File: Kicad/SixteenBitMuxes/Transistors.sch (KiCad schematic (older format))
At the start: 20 parts, among them Q1 PN2222A, Q10 2SC1815, Q12 S9013, Q14 S9018, Q15 BC848B, Q16 2SC1623, Q17 MPSA18, Q19 2N5088, Q2 MMBT3904, Q3 MMBT5551L, Q4 MMBTA42, Q5 BC807, Q6 BC846, Q7 BC847B, Q8 BC847C, Q9 C945, U8 CD4067BM, U9 CD4067BM

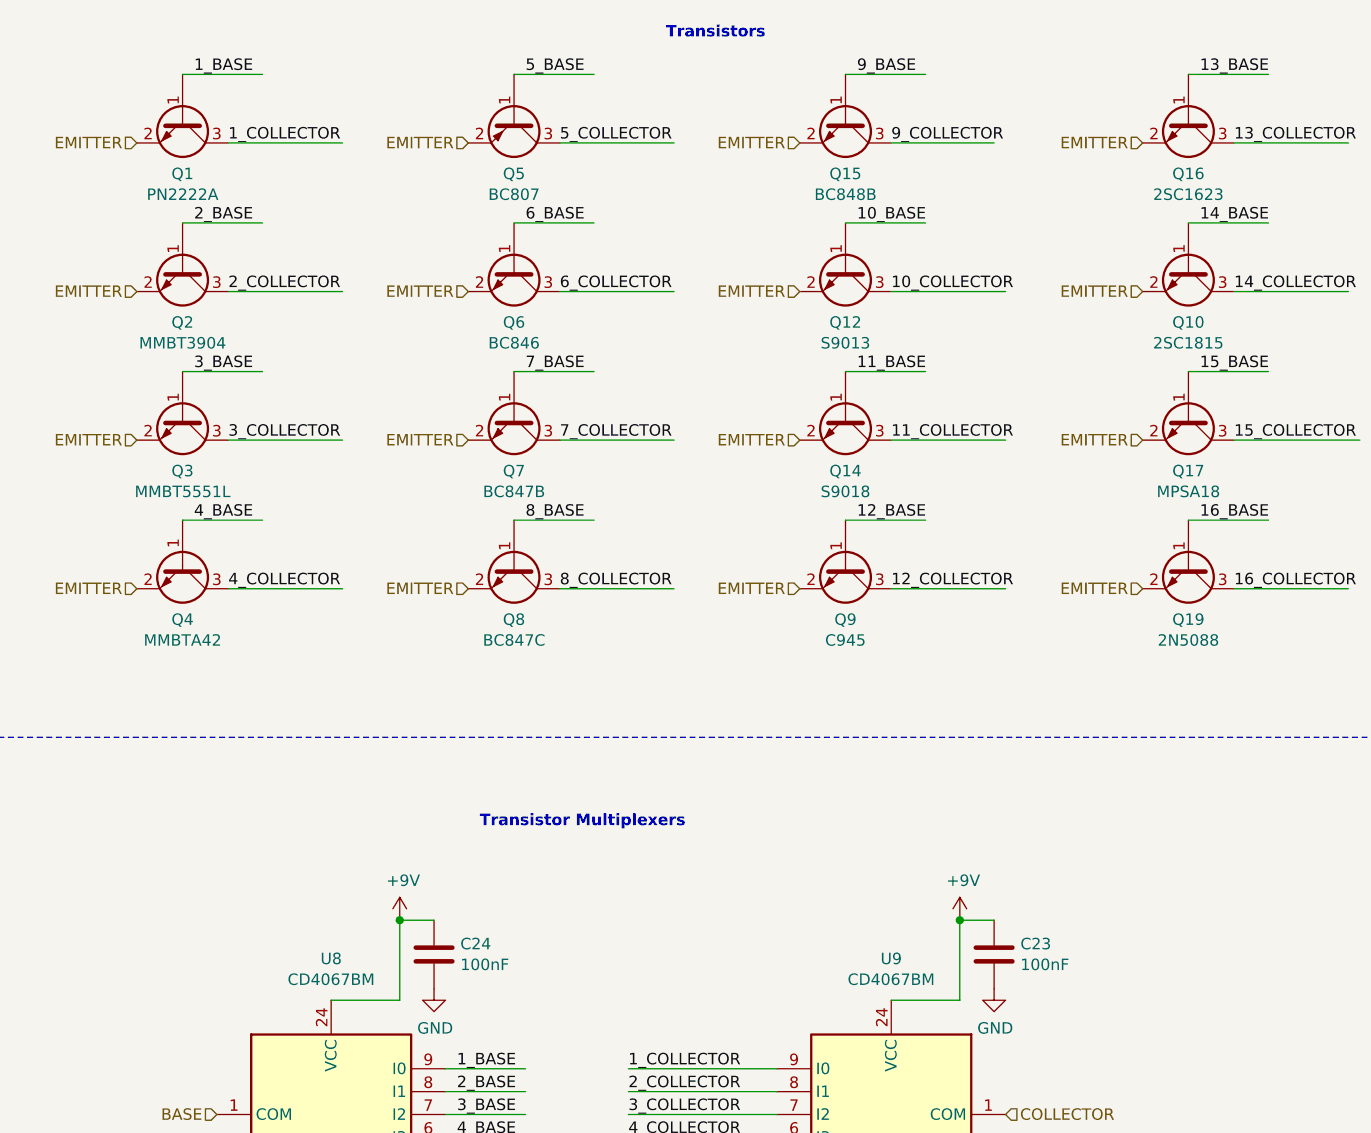
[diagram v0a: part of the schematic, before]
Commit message: PCB Logo/texts
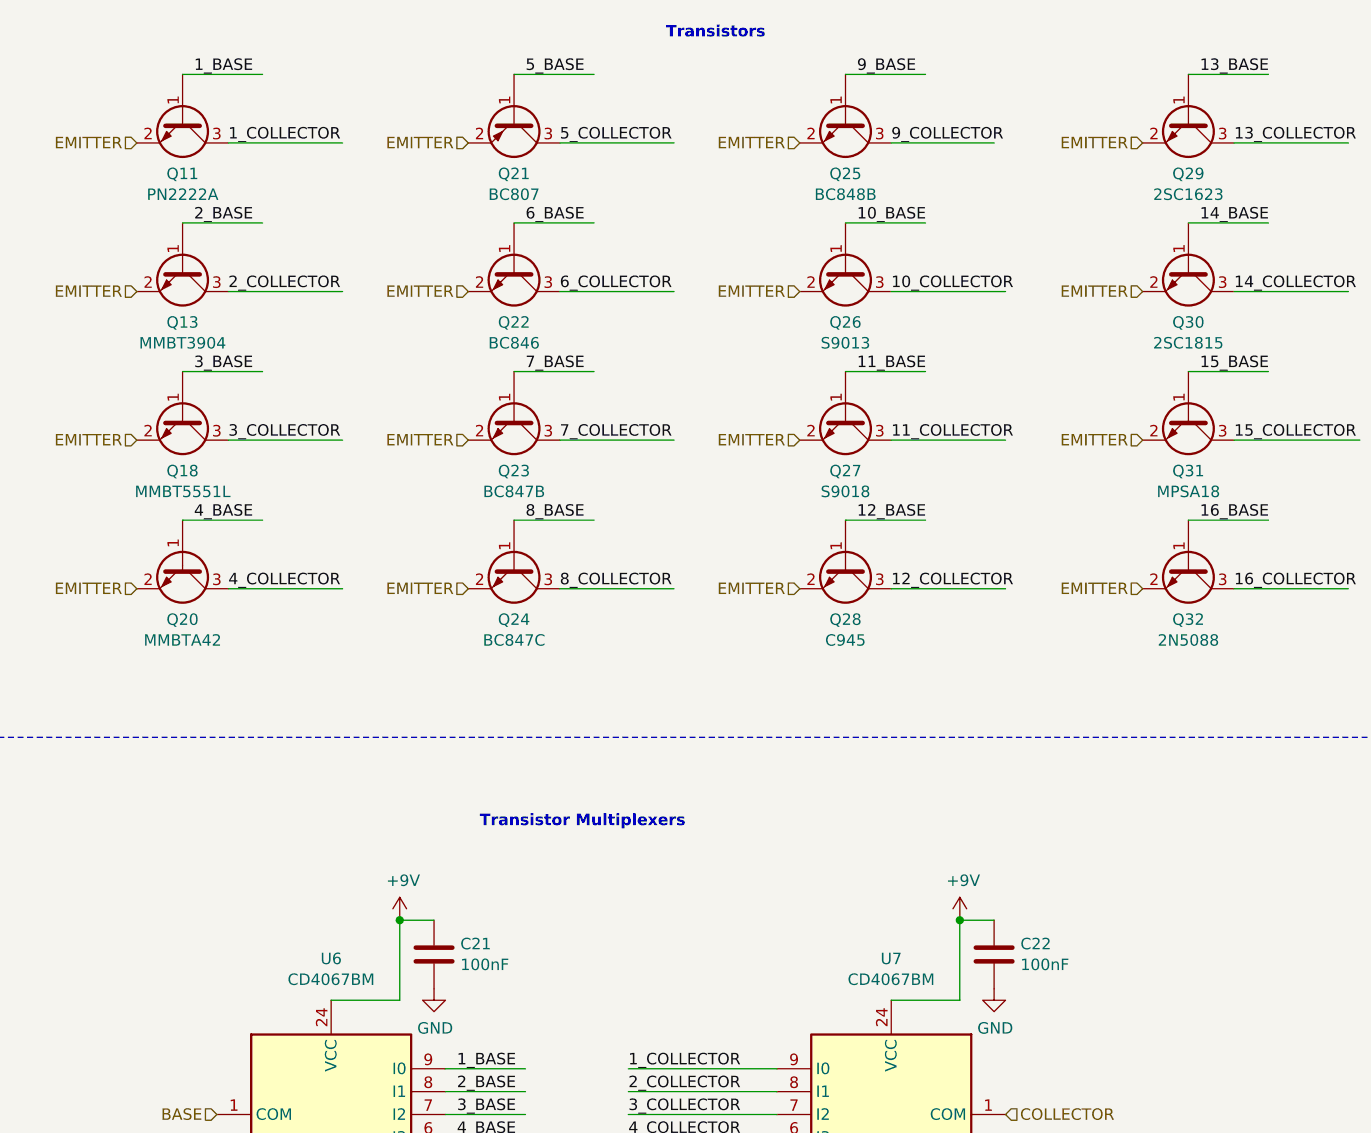
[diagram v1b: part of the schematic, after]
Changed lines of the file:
@@
 $Descr A4 11693 8268
 encoding utf-8
-Sheet 8 9
+Sheet 6 9
 Title "Guitar Pedal Effect Fuzz Digitally Controlled"
 Date "2020-04-07"
@@
 AR Path="/5F9746B8/5EA993A8" Ref="Q24"  Part="1"
 AR Path="/5ED1AB26/5EA993A8" Ref="Q20"  Part="1"
-F 0 "Q4" V 1835 3400 50  0000 C CNN
+F 0 "Q20" V 1835 3400 50  0000 C CNN
 F 1 "MMBTA42" V 1926 3400 50  0000 C CNN
 F 2 "Package_TO_SOT_SMD:SOT-23_Handsoldering" H 1800 3325 50  0001 L CIN
@@
 AR Path="/5F9746B8/5EA993B4" Ref="Q39"  Part="1"
 AR Path="/5ED1AB26/5EA993B4" Ref="Q32"  Part="1"
-F 0 "Q19" V 6235 3400 50  0000 C CNN
+F 0 "Q32" V 6235 3400 50  0000 C CNN
 F 1 "2N5088" V 6326 3400 50  0000 C CNN
 F 2 "Package_TO_SOT_THT:TO-92_Inline" H 6200 3325 50  0001 L CIN
@@
 AR Path="/5F9746B8/5EA993C0" Ref="Q37"  Part="1"
 AR Path="/5ED1AB26/5EA993C0" Ref="Q31"  Part="1"
-F 0 "Q17" V 6235 2750 50  0000 C CNN
+F 0 "Q31" V 6235 2750 50  0000 C CNN
 F 1 "MPSA18" V 6326 2750 50  0000 C CNN
 F 2 "Package_TO_SOT_THT:TO-92_Inline" H 6200 2675 50  0001 L CIN
@@
 AR Path="/5F9746B8/5EA993CD" Ref="Q36"  Part="1"
 AR Path="/5ED1AB26/5EA993CD" Ref="Q29"  Part="1"
-F 0 "Q16" V 6235 1450 50  0000 C CNN
+F 0 "Q29" V 6235 1450 50  0000 C CNN
 F 1 "2SC1623" V 6326 1450 50  0000 C CNN
 F 2 "Package_TO_SOT_SMD:SOT-23_Handsoldering" H 6200 1550 50  0001 C CNN
@@
 AR Path="/5F9746B8/5EA993FC" Ref="Q28"  Part="1"
 AR Path="/5ED1AB26/5EA993FC" Ref="Q24"  Part="1"
-F 0 "Q8" V 3285 3400 50  0000 C CNN
+F 0 "Q24" V 3285 3400 50  0000 C CNN
 F 1 "BC847C" V 3376 3400 50  0000 C CNN
 F 2 "Package_TO_SOT_SMD:SOT-23_Handsoldering" H 3250 3325 50  0001 L CIN
@@
 AR Path="/5F9746B8/5EA99402" Ref="Q27"  Part="1"
 AR Path="/5ED1AB26/5EA99402" Ref="Q23"  Part="1"
-F 0 "Q7" V 3285 2750 50  0000 C CNN
+F 0 "Q23" V 3285 2750 50  0000 C CNN
 F 1 "BC847B" V 3376 2750 50  0000 C CNN
 F 2 "Package_TO_SOT_SMD:SOT-23_Handsoldering" H 3250 2850 50  0001 C CNN
@@
 AR Path="/5F9746B8/5EA99408" Ref="Q26"  Part="1"
 AR Path="/5ED1AB26/5EA99408" Ref="Q22"  Part="1"
-F 0 "Q6" V 3285 2100 50  0000 C CNN
+F 0 "Q22" V 3285 2100 50  0000 C CNN
 F 1 "BC846" V 3376 2100 50  0000 C CNN
 F 2 "Package_TO_SOT_SMD:SOT-23_Handsoldering" H 3250 2025 50  0001 L CIN
@@
 AR Path="/5F9746B8/5EA9940E" Ref="Q25"  Part="1"
 AR Path="/5ED1AB26/5EA9940E" Ref="Q21"  Part="1"
-F 0 "Q5" V 3285 1450 50  0000 C CNN
+F 0 "Q21" V 3285 1450 50  0000 C CNN
 F 1 "BC807" V 3376 1450 50  0000 C CNN
 F 2 "Package_TO_SOT_SMD:SOT-23_Handsoldering" H 3250 1375 50  0001 L CIN
@@
 AR Path="/5F9746B8/5EA9951D" Ref="#PWR083"  Part="1"
 AR Path="/5ED1AB26/5EA9951D" Ref="#PWR0102"  Part="1"
-F 0 "#PWR055" H 2700 5000 50  0001 C CNN
+F 0 "#PWR0102" H 2700 5000 50  0001 C CNN
 F 1 "GND" H 2705 5077 50  0000 C CNN
 F 2 "" H 2700 5250 50  0001 C CNN
@@
 AR Path="/5F9746B8/5EA99637" Ref="Q23"  Part="1"
 AR Path="/5ED1AB26/5EA99637" Ref="Q18"  Part="1"
-F 0 "Q3" V 1835 2750 50  0000 C CNN
+F 0 "Q18" V 1835 2750 50  0000 C CNN
 F 1 "MMBT5551L" V 1926 2750 50  0000 C CNN
 F 2 "Package_TO_SOT_SMD:SOT-23_Handsoldering" H 1800 2675 50  0001 L CIN
@@
 AR Path="/5F9746B8/5EA99643" Ref="Q22"  Part="1"
 AR Path="/5ED1AB26/5EA99643" Ref="Q13"  Part="1"
-F 0 "Q2" V 1835 2100 50  0000 C CNN
+F 0 "Q13" V 1835 2100 50  0000 C CNN
 F 1 "MMBT3904" V 1926 2100 50  0000 C CNN
 F 2 "Package_TO_SOT_SMD:SOT-23_Handsoldering" H 1800 2025 50  0001 L CIN
@@
 AR Path="/5F9746B8/5F014460" Ref="Q30"  Part="1"
 AR Path="/5ED1AB26/5F014460" Ref="Q30"  Part="1"
-F 0 "Q10" V 6235 2100 50  0000 C CNN
+F 0 "Q30" V 6235 2100 50  0000 C CNN
 F 1 "2SC1815" V 6326 2100 50  0000 C CNN
 F 2 "Package_TO_SOT_SMD:SOT-23_Handsoldering" H 6200 2025 50  0001 L CIN
@@
 AR Path="/5F9746B8/5F02F005" Ref="Q29"  Part="1"
 AR Path="/5ED1AB26/5F02F005" Ref="Q28"  Part="1"
-F 0 "Q9" V 4735 3400 50  0000 C CNN
+F 0 "Q28" V 4735 3400 50  0000 C CNN
 F 1 "C945" V 4826 3400 50  0000 C CNN
 F 2 "Package_TO_SOT_SMD:SOT-23_Handsoldering" H 4700 3500 50  0001 C CNN
@@
 AR Path="/5F9746B8/5EA9963D" Ref="Q21"  Part="1"
 AR Path="/5ED1AB26/5EA9963D" Ref="Q11"  Part="1"
-F 0 "Q1" V 1835 1450 50  0000 C CNN
+F 0 "Q11" V 1835 1450 50  0000 C CNN
 F 1 "PN2222A" V 1926 1450 50  0000 C CNN
 F 2 "Package_TO_SOT_SMD:SOT-23_Handsoldering" H 1800 1375 50  0001 L CIN
@@
 AR Path="/5F9746B8/5EA993C7" Ref="Q35"  Part="1"
 AR Path="/5ED1AB26/5EA993C7" Ref="Q25"  Part="1"
-F 0 "Q15" V 4735 1450 50  0000 C CNN
+F 0 "Q25" V 4735 1450 50  0000 C CNN
 F 1 "BC848B" V 4826 1450 50  0000 C CNN
 F 2 "Package_TO_SOT_SMD:SOT-23_Handsoldering" H 4700 1375 50  0001 L CIN
@@
 AR Path="/5F9746B8/5EA993D3" Ref="Q34"  Part="1"
 AR Path="/5ED1AB26/5EA993D3" Ref="Q27"  Part="1"
-F 0 "Q14" V 4735 2750 50  0000 C CNN
+F 0 "Q27" V 4735 2750 50  0000 C CNN
 F 1 "S9018" V 4826 2750 50  0000 C CNN
 F 2 "Package_TO_SOT_SMD:SOT-23_Handsoldering" H 4700 2850 50  0001 C CNN
@@
 AR Path="/5F9746B8/5EA993DF" Ref="Q32"  Part="1"
 AR Path="/5ED1AB26/5EA993DF" Ref="Q26"  Part="1"
-F 0 "Q12" V 4735 2100 50  0000 C CNN
+F 0 "Q26" V 4735 2100 50  0000 C CNN
 F 1 "S9013" V 4826 2100 50  0000 C CNN
 F 2 "Package_TO_SOT_SMD:SOT-23_Handsoldering" H 4700 2200 50  0001 C CNN
@@
 AR Path="/5E9AE796/5EA4E538" Ref="U9"  Part="1"
 AR Path="/5ED1AB26/5EA4E538" Ref="U7"  Part="1"
-F 0 "U9" H 4700 7481 50  0000 C CNN
+F 0 "U7" H 4700 7481 50  0000 C CNN
 F 1 "CD4067BM" H 4700 7390 50  0000 C CNN
 F 2 "Package_SO:SOIC-24W_7.5x15.4mm_P1.27mm" H 5600 5300 50  0001 C CIN
@@
 AR Path="/5E9AE796/5EA3E429" Ref="U8"  Part="1"
 AR Path="/5ED1AB26/5EA3E429" Ref="U6"  Part="1"
-F 0 "U8" H 2250 7481 50  0000 C CNN
+F 0 "U6" H 2250 7481 50  0000 C CNN
 F 1 "CD4067BM" H 2250 7390 50  0000 C CNN
 F 2 "Package_SO:SOIC-24W_7.5x15.4mm_P1.27mm" H 3150 5300 50  0001 C CIN
@@
 AR Path="/5F9746B8/5EAD9CE0" Ref="#PWR0129"  Part="1"
 AR Path="/5ED1AB26/5EAD9CE0" Ref="#PWR0109"  Part="1"
-F 0 "#PWR0144" H 2550 4800 50  0001 C CNN
+F 0 "#PWR0109" H 2550 4800 50  0001 C CNN
 F 1 "+9V" H 2565 5123 50  0000 C CNN
 F 2 "" H 2550 4950 50  0001 C CNN
@@
 AR Path="/5F9746B8/5EA99533" Ref="C31"  Part="1"
 AR Path="/5ED1AB26/5EA99533" Ref="C21"  Part="1"
-F 0 "C24" H 2815 5146 50  0000 L CNN
+F 0 "C21" H 2815 5146 50  0000 L CNN
 F 1 "100nF" H 2815 5055 50  0000 L CNN
 F 2 "Capacitor_SMD:C_0805_2012Metric_Pad1.15x1.40mm_HandSolder" H 2738 4950 50  0001 C CNN
@@
 AR Path="/5F9746B8/5EC11EC1" Ref="#PWR?"  Part="1"
 AR Path="/5ED1AB26/5EC11EC1" Ref="#PWR0120"  Part="1"
-F 0 "#PWR0132" H 2250 7150 50  0001 C CNN
+F 0 "#PWR0120" H 2250 7150 50  0001 C CNN
 F 1 "GND" H 2255 7227 50  0000 C CNN
 F 2 "" H 2250 7400 50  0001 C CNN
@@
 AR Path="/5F9746B8/5ECDD1BA" Ref="#PWR?"  Part="1"
 AR Path="/5ED1AB26/5ECDD1BA" Ref="#PWR0121"  Part="1"
-F 0 "#PWR0133" H 5000 4800 50  0001 C CNN
+F 0 "#PWR0121" H 5000 4800 50  0001 C CNN
 F 1 "+9V" H 5015 5123 50  0000 C CNN
 F 2 "" H 5000 4950 50  0001 C CNN
@@
 AR Path="/5F9746B8/5ECDF6D6" Ref="C?"  Part="1"
 AR Path="/5ED1AB26/5ECDF6D6" Ref="C22"  Part="1"
-F 0 "C23" H 5265 5146 50  0000 L CNN
+F 0 "C22" H 5265 5146 50  0000 L CNN
 F 1 "100nF" H 5265 5055 50  0000 L CNN
 F 2 "Capacitor_SMD:C_0805_2012Metric_Pad1.15x1.40mm_HandSolder" H 5188 4950 50  0001 C CNN
@@
 AR Path="/5F9746B8/5ECE05A8" Ref="#PWR?"  Part="1"
 AR Path="/5ED1AB26/5ECE05A8" Ref="#PWR0128"  Part="1"
-F 0 "#PWR0134" H 5150 5000 50  0001 C CNN
+F 0 "#PWR0128" H 5150 5000 50  0001 C CNN
 F 1 "GND" H 5155 5077 50  0000 C CNN
 F 2 "" H 5150 5250 50  0001 C CNN
@@
 AR Path="/5F9746B8/5ECEC63C" Ref="#PWR?"  Part="1"
 AR Path="/5ED1AB26/5ECEC63C" Ref="#PWR0129"  Part="1"
-F 0 "#PWR0135" H 4700 7150 50  0001 C CNN
+F 0 "#PWR0129" H 4700 7150 50  0001 C CNN
 F 1 "GND" H 4705 7227 50  0000 C CNN
 F 2 "" H 4700 7400 50  0001 C CNN
@@
 AR Path="/5F9746B8/5EEBED85" Ref="#PWR?"  Part="1"
 AR Path="/5ED1AB26/5EEBED85" Ref="#PWR0130"  Part="1"
-F 0 "#PWR0137" H 1750 6650 50  0001 C CNN
+F 0 "#PWR0130" H 1750 6650 50  0001 C CNN
 F 1 "GND" H 1755 6727 50  0000 C CNN
 F 2 "" H 1750 6900 50  0001 C CNN
@@
 AR Path="/5F9746B8/5EEBF1A5" Ref="#PWR?"  Part="1"
 AR Path="/5ED1AB26/5EEBF1A5" Ref="#PWR0131"  Part="1"
-F 0 "#PWR0138" H 5200 6650 50  0001 C CNN
+F 0 "#PWR0131" H 5200 6650 50  0001 C CNN
 F 1 "GND" H 5205 6727 50  0000 C CNN
 F 2 "" H 5200 6900 50  0001 C CNN

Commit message: EEprom + PCB changes
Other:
- moved on the sheet: C21, C22, Q11, Q13, Q18, Q20, Q21, Q22, Q23, Q24, Q25, Q26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
